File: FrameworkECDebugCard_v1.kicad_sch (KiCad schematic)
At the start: 24 parts, among them P1 USB_C_Plug_USB2.0, P2 USB_B_Micro, U1 FT230XS

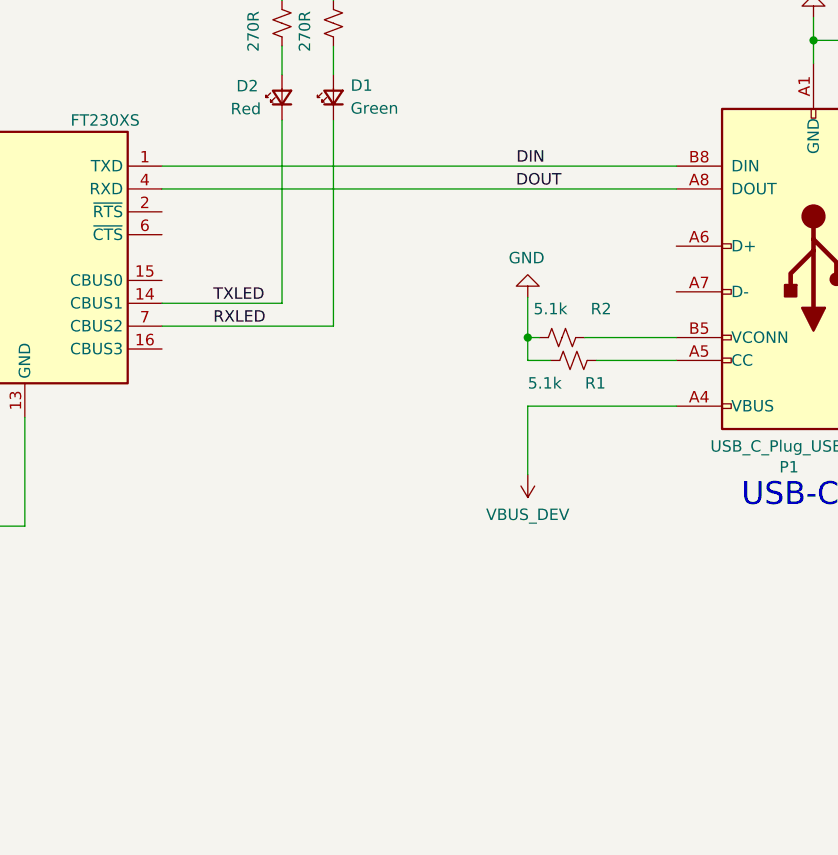
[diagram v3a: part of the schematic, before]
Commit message: Add a 1x5 header to break out the EC/FTDI pins
This header uses the SparkFun "LOCK" footprint, which should
allow me to click in a header without soldering it down.
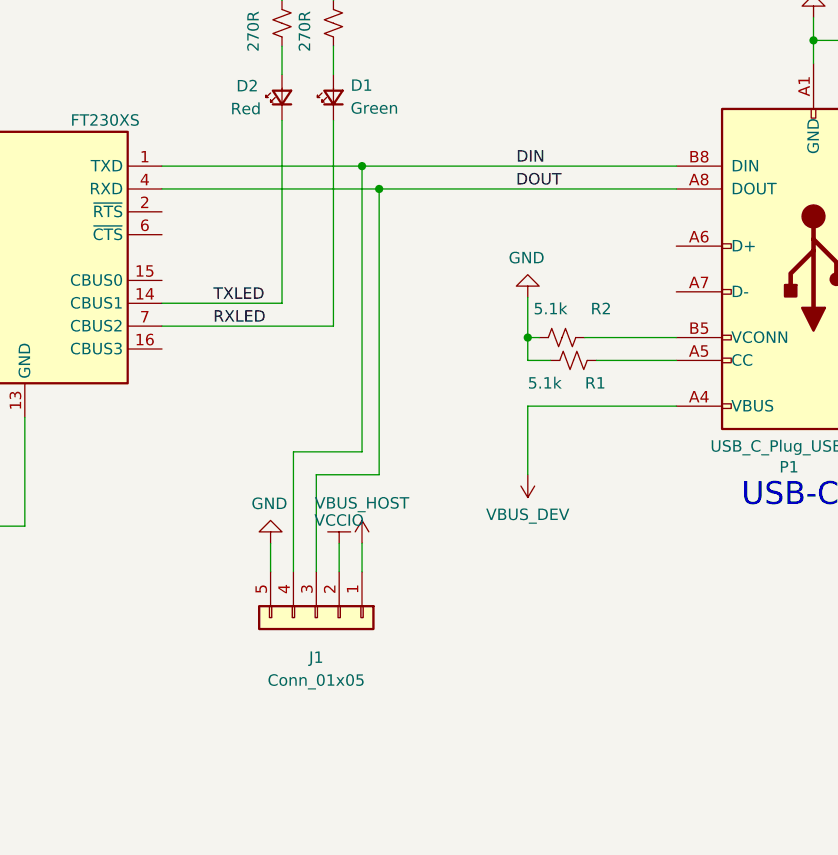
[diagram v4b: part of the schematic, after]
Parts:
- added J1: Conn_01x05, FrameworkECDebugCard_v1:1X05_LOCK, symbol Connector_Generic:Conn_01x05
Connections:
- net DIN: now also J1.4 (Pin_4)
- net DOUT: now also J1.3 (Pin_3)
- net GND: now also J1.5 (Pin_5)
- net VBUS_HOST: now also J1.1 (Pin_1)
- net VCCIO: now also J1.2 (Pin_2)
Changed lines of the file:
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@@
   (junction (at 144.145 63.5) (diameter 0) (color 0 0 0 0)
   )
+  (junction (at 127.635 46.99) (diameter 0) (color 0 0 0 0)
+  )
   (junction (at 54.61 36.83) (diameter 0) (color 0 0 0 0)
   )
@@
   (junction (at 34.925 102.87) (diameter 0) (color 0 0 0 0)
   )
+  (junction (at 125.73 44.45) (diameter 0) (color 0 0 0 0)
+  )
   (wire (pts (xy 116.84 31.115) (xy 116.84 34.29))
     (stroke (width 0) (type default) (color 0 0 0 0))
@@
     (stroke (width 0) (type default) (color 0 0 0 0))
   )
+  (wire (pts (xy 123.19 86.36) (xy 123.19 89.535))
+    (stroke (width 0) (type default) (color 0 0 0 0))
+  )
   (wire (pts (xy 67.945 57.15) (xy 62.23 57.15))
     (stroke (width 0) (type default) (color 0 0 0 0))
@@
     (stroke (width 0) (type default) (color 0 0 0 0))
   )
-  (wire (pts (xy 103.505 46.99) (xy 160.655 46.99))
+  (wire (pts (xy 103.505 46.99) (xy 127.635 46.99))
+    (stroke (width 0) (type default) (color 0 0 0 0))
+  )
+  (wire (pts (xy 125.73 86.36) (xy 125.73 89.535))
     (stroke (width 0) (type default) (color 0 0 0 0))
   )
@@
     (stroke (width 0) (type default) (color 0 0 0 0))
   )
+  (wire (pts (xy 125.73 44.45) (xy 125.73 76.2))
+    (stroke (width 0) (type default) (color 0 0 0 0))
+  )
+  (wire (pts (xy 125.73 76.2) (xy 118.11 76.2))
+    (stroke (width 0) (type default) (color 0 0 0 0))
+  )
   (wire (pts (xy 146.685 66.04) (xy 144.145 66.04))
     (stroke (width 0) (type default) (color 0 0 0 0))
@@
     (stroke (width 0) (type default) (color 0 0 0 0))
   )
+  (wire (pts (xy 115.57 86.36) (xy 115.57 89.535))
+    (stroke (width 0) (type default) (color 0 0 0 0))
+  )
   (wire (pts (xy 40.005 66.04) (xy 40.005 69.215))
     (stroke (width 0) (type default) (color 0 0 0 0))
@@
     (stroke (width 0) (type default) (color 0 0 0 0))
   )
+  (wire (pts (xy 127.635 46.99) (xy 127.635 78.74))
+    (stroke (width 0) (type default) (color 0 0 0 0))
+  )
   (wire (pts (xy 88.265 72.39) (xy 88.265 84.455))
     (stroke (width 0) (type default) (color 0 0 0 0))
@@
     (stroke (width 0) (type default) (color 0 0 0 0))
   )
-  (wire (pts (xy 103.505 44.45) (xy 160.655 44.45))
+  (wire (pts (xy 103.505 44.45) (xy 125.73 44.45))
     (stroke (width 0) (type default) (color 0 0 0 0))
   )
@@
     (stroke (width 0) (type default) (color 0 0 0 0))
   )
+  (wire (pts (xy 118.11 76.2) (xy 118.11 89.535))
+    (stroke (width 0) (type default) (color 0 0 0 0))
+  )
   (wire (pts (xy 160.655 71.12) (xy 144.145 71.12))
     (stroke (width 0) (type default) (color 0 0 0 0))
@@
     (stroke (width 0) (type default) (color 0 0 0 0))
   )
+  (wire (pts (xy 120.65 78.74) (xy 120.65 89.535))
+    (stroke (width 0) (type default) (color 0 0 0 0))
+  )
   (wire (pts (xy 45.72 46.99) (xy 55.88 46.99))
     (stroke (width 0) (type default) (color 0 0 0 0))
   )
+  (wire (pts (xy 127.635 46.99) (xy 160.655 46.99))
+    (stroke (width 0) (type default) (color 0 0 0 0))
+  )
   (wire (pts (xy 122.555 19.685) (xy 122.555 26.035))
     (stroke (width 0) (type default) (color 0 0 0 0))
@@
   )
   (wire (pts (xy 145.415 63.5) (xy 144.145 63.5))
+    (stroke (width 0) (type default) (color 0 0 0 0))
+  )
+  (wire (pts (xy 125.73 44.45) (xy 160.655 44.45))
+    (stroke (width 0) (type default) (color 0 0 0 0))
+  )
+  (wire (pts (xy 127.635 78.74) (xy 120.65 78.74))
     (stroke (width 0) (type default) (color 0 0 0 0))
   )
@@
     (pin "1")
   )
+  (symbol (lib_id "power:GND") (at 115.57 86.36 180) (unit 1)
+    (in_bom yes) (on_board yes)
+    (property "Reference" "#PWR0111" (id 0) (at 115.57 80.01 0)
+      (effects (font (size 1.27 1.27)) hide)
+    )
+    (property "Value" "GND" (id 1) (at 115.443 81.9658 0))
+    (property "Footprint" "" (id 2) (at 115.57 86.36 0)
+      (effects (font (size 1.27 1.27)) hide)
+    )
+    (property "Datasheet" "" (id 3) (at 115.57 86.36 0)
+      (effects (font (size 1.27 1.27)) hide)
+    )
+    (pin "1")
+  )
   (symbol (lib_id "Device:LED_Small") (at 116.84 36.83 90) (unit 1)
     (in_bom yes) (on_board yes)
@@
     (pin "1")
     (pin "2")
+  )
+  (symbol (lib_name "VCCIO_1") (lib_id "FrameworkECDebugCard_v1-rescue:VCCIO") (at 123.19 86.36 0) (unit 1)
+    (in_bom yes) (on_board yes)
+    (property "Reference" "#PWR0112" (id 0) (at 123.19 90.17 0)
+      (effects (font (size 1.27 1.27)) hide)
+    )
+    (property "Value" "VCCIO" (id 1) (at 123.19 83.82 0))
+    (property "Footprint" "" (id 2) (at 123.19 86.36 0)
+      (effects (font (size 1.27 1.27)) hide)
+    )
+    (property "Datasheet" "" (id 3) (at 123.19 86.36 0)
+      (effects (font (size 1.27 1.27)) hide)
+    )
+    (pin "1")
   )
   (symbol (lib_id "power:GND") (at 26.67 73.025 0) (unit 1)
@@
     (pin "2")
   )
+  (symbol (lib_id "FrameworkECDebugCard_v1-rescue:VBUS_HOST") (at 125.73 86.36 0) (unit 1)
+    (in_bom yes) (on_board yes)
+    (property "Reference" "#PWR0110" (id 0) (at 125.73 90.17 0)
+      (effects (font (size 1.27 1.27)) hide)
+    )
+    (property "Value" "VBUS_HOST" (id 1) (at 125.73 81.915 0))
+    (property "Footprint" "" (id 2) (at 125.73 86.36 0)
+      (effects (font (size 1.27 1.27)) hide)
+    )
+    (property "Datasheet" "" (id 3) (at 125.73 86.36 0)
+      (effects (font (size 1.27 1.27)) hide)
+    )
+    (pin "1")
+  )
   (symbol (lib_id "Connector:USB_B_Micro") (at 24.765 44.45 0) (unit 1)
     (in_bom yes) (on_board yes) (fields_autoplaced)
@@
     )
     (pin "1")
+  )
+  (symbol (lib_id "Connector_Generic:Conn_01x05") (at 120.65 94.615 270) (unit 1)
+    (in_bom no) (on_board yes) (fields_autoplaced)
+    (property "Reference" "J1" (id 0) (at 120.65 99.06 90))
+    (property "Value" "Conn_01x05" (id 1) (at 120.65 101.6 90))
+    (property "Footprint" "FrameworkECDebugCard_v1:1X05_LOCK" (id 2) (at 120.65 94.615 0)
+      (effects (font (size 1.27 1.27)) hide)
+    )
+    (property "Datasheet" "~" (id 3) (at 120.65 94.615 0)
+      (effects (font (size 1.27 1.27)) hide)
+    )
+    (pin "1")
+    (pin "2")
+    (pin "3")
+    (pin "4")
+    (pin "5")
   )
   (symbol (lib_id "Device:C_Small") (at 41.91 111.125 0) (unit 1)
@@
       (reference "#PWR0109") (unit 1) (value "VBUS_HOST") (footprint "")
     )
+    (path "/972f110e-25e6-42e3-895b-1f08816f389b"
+      (reference "#PWR0110") (unit 1) (value "VBUS_HOST") (footprint "")
+    )
+    (path "/0cefe424-2c69-440e-bfa1-43f7b326a942"
+      (reference "#PWR0111") (unit 1) (value "GND") (footprint "")
+    )
+    (path "/41397ac6-deec-4684-a1fe-fc97df4bb74d"
+      (reference "#PWR0112") (unit 1) (value "VCCIO") (footprint "")
+    )
     (path "/e4410938-748d-4f87-a5a0-2f41e55e999c"
       (reference "C1") (unit 1) (value "100nf") (footprint "Capacitor_SMD:C_0402_1005Metric")
@@
       (reference "H2") (unit 1) (value "MountingHole") (footprint "MountingHole:MountingHole_2.2mm_M2")
     )
+    (path "/d0726bc2-9333-4c1c-8a2c-af2615eef0e6"
+      (reference "J1") (unit 1) (value "Conn_01x05") (footprint "FrameworkECDebugCard_v1:1X05_LOCK")
+    )
     (path "/00000000-0000-0000-0000-00005fd76bc6"

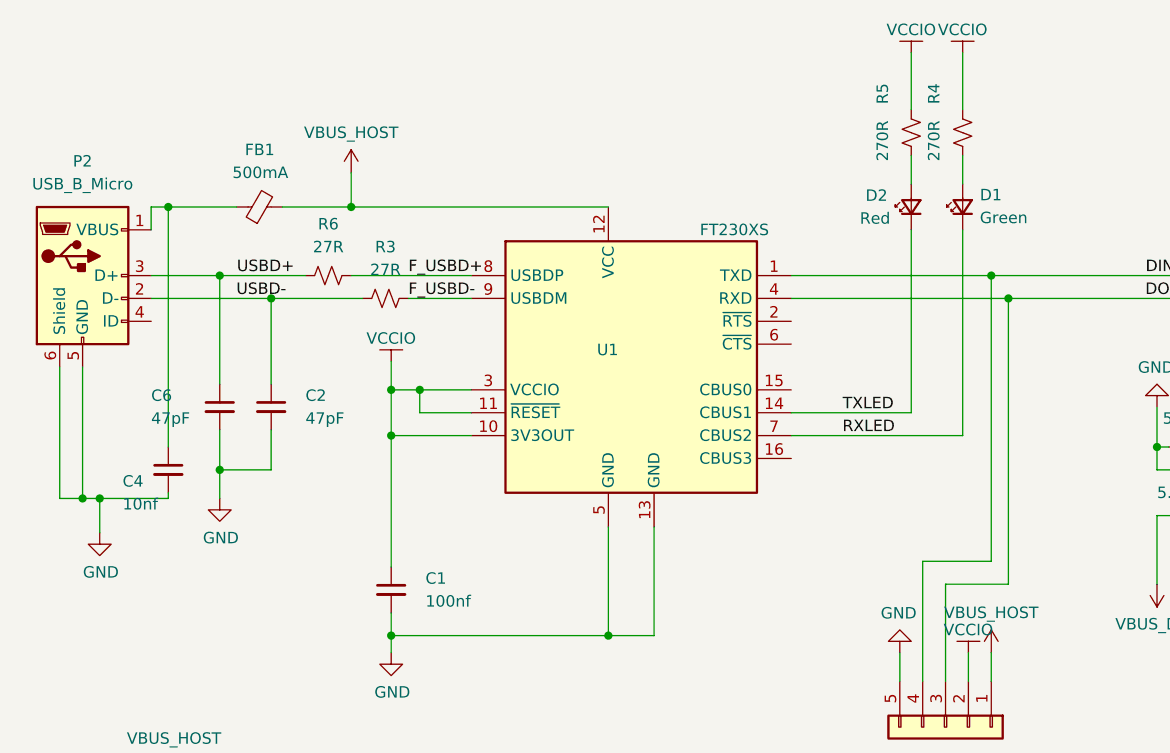
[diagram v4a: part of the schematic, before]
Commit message: Re-route everything to avoid B.Cu cuts across diff pair
Switched the positions of the TX and RX LEDs to match which side of the
chip they're on. Significantly re-routed TX/RX. Added via stitching.

The ground planes are much more contiguous, except for U1 pad 5 which
connects to GND on the back with a via.

(Kieran's suggestion was to remove the lines on the back that cut
horizontally across the differential pair; I don't know if having
RXLED's sink next to the diff pair will be a problem.)

Re-version the card to "EC Card 2"
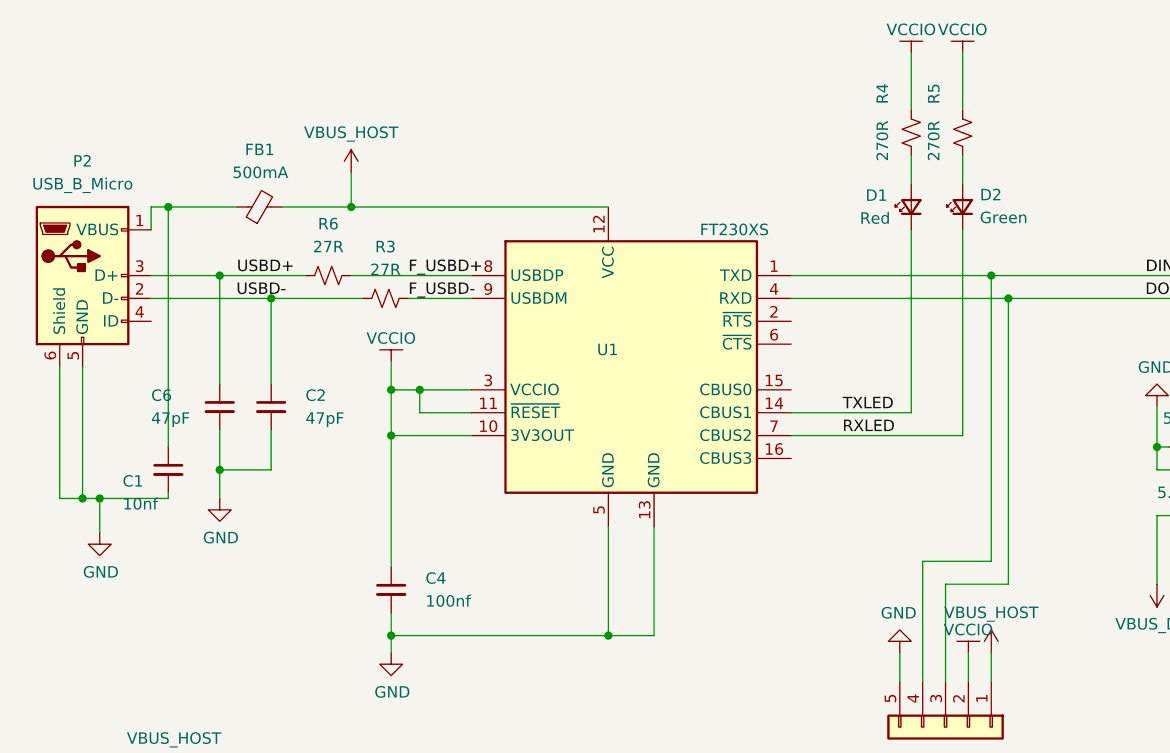
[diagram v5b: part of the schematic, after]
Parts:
- renumbered C4 to C1, C1 to C4, D2 to D1, D1 to D2, R5 to R4, R4 to R5
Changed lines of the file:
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@@
   (symbol (lib_id "Device:LED_Small") (at 116.84 36.83 90) (unit 1)
     (in_bom yes) (on_board yes)
-    (property "Reference" "D2" (id 0) (at 111.76 35.56 90)
+    (property "Reference" "D1" (id 0) (at 111.76 35.56 90)
       (effects (font (size 1.27 1.27)) (justify right))
     )
@@
   (symbol (lib_id "Device:LED_Small") (at 122.555 36.83 90) (unit 1)
     (in_bom yes) (on_board yes) (fields_autoplaced)
-    (property "Reference" "D1" (id 0) (at 124.46 35.4964 90)
+    (property "Reference" "D2" (id 0) (at 124.46 35.4964 90)
       (effects (font (size 1.27 1.27)) (justify right))
     )
@@
   (symbol (lib_id "Device:R_Small_US") (at 116.84 28.575 0) (unit 1)
     (in_bom yes) (on_board yes)
-    (property "Reference" "R5" (id 0) (at 113.665 25.4 90)
+    (property "Reference" "R4" (id 0) (at 113.665 25.4 90)
       (effects (font (size 1.27 1.27)) (justify left))
     )
@@
   (symbol (lib_id "Device:C_Small") (at 59.055 79.375 0) (unit 1)
     (in_bom yes) (on_board yes) (fields_autoplaced)
-    (property "Reference" "C1" (id 0) (at 62.865 78.1049 0)
+    (property "Reference" "C4" (id 0) (at 62.865 78.1049 0)
       (effects (font (size 1.27 1.27)) (justify left))
     )
@@
   (symbol (lib_id "Device:C_Small") (at 34.29 66.04 0) (unit 1)
     (in_bom yes) (on_board yes)
-    (property "Reference" "C4" (id 0) (at 29.21 67.31 0)
+    (property "Reference" "C1" (id 0) (at 29.21 67.31 0)
       (effects (font (size 1.27 1.27)) (justify left))
     )
@@
   (symbol (lib_id "Device:R_Small_US") (at 122.555 28.575 0) (unit 1)
     (in_bom yes) (on_board yes)
-    (property "Reference" "R4" (id 0) (at 119.38 25.4 90)
+    (property "Reference" "R5" (id 0) (at 119.38 25.4 90)
       (effects (font (size 1.27 1.27)) (justify left))
     )
@@
       (reference "#PWR0112") (unit 1) (value "VCCIO") (footprint "")
     )
-    (path "/e4410938-748d-4f87-a5a0-2f41e55e999c"
-      (reference "C1") (unit 1) (value "100nf") (footprint "Capacitor_SMD:C_0402_1005Metric")
+    (path "/e88ed97c-5f7f-4fa6-b202-1f3880388383"
+      (reference "C1") (unit 1) (value "10nf") (footprint "Capacitor_SMD:C_0402_1005Metric")
     )
     (path "/685f0971-12c4-4d07-8eec-3ff16ff9a7d3"
@@
       (reference "C3") (unit 1) (value "100nf") (footprint "Capacitor_SMD:C_0402_1005Metric")
     )
-    (path "/e88ed97c-5f7f-4fa6-b202-1f3880388383"
-      (reference "C4") (unit 1) (value "10nf") (footprint "Capacitor_SMD:C_0402_1005Metric")
+    (path "/e4410938-748d-4f87-a5a0-2f41e55e999c"
+      (reference "C4") (unit 1) (value "100nf") (footprint "Capacitor_SMD:C_0402_1005Metric")
     )
     (path "/d393b8c4-8105-4600-aeed-08d8efde382f"
@@
       (reference "C6") (unit 1) (value "47pF") (footprint "Capacitor_SMD:C_0402_1005Metric")
     )
+    (path "/2326b3ba-1742-4f36-87f7-22991a003d68"
+      (reference "D1") (unit 1) (value "Red") (footprint "LED_SMD:LED_0603_1608Metric")
+    )
     (path "/951a9737-1abd-4cc1-a961-022d0a301f2c"
-      (reference "D1") (unit 1) (value "Green") (footprint "LED_SMD:LED_0603_1608Metric")
-    )
-    (path "/2326b3ba-1742-4f36-87f7-22991a003d68"
-      (reference "D2") (unit 1) (value "Red") (footprint "LED_SMD:LED_0603_1608Metric")
+      (reference "D2") (unit 1) (value "Green") (footprint "LED_SMD:LED_0603_1608Metric")
     )
     (path "/91d38762-eed1-4640-8cf2-f727d0ea908c"
@@
       (reference "R3") (unit 1) (value "27R") (footprint "Resistor_SMD:R_0402_1005Metric")
     )
+    (path "/dd063de5-da3d-49de-a899-532aa51b8a7c"
+      (reference "R4") (unit 1) (value "270R") (footprint "Resistor_SMD:R_0402_1005Metric")
+    )
     (path "/f4b69b4c-b4ac-4a4e-8c9e-77f4e7698670"
-      (reference "R4") (unit 1) (value "270R") (footprint "Resistor_SMD:R_0402_1005Metric")
-    )
-    (path "/dd063de5-da3d-49de-a899-532aa51b8a7c"
       (reference "R5") (unit 1) (value "270R") (footprint "Resistor_SMD:R_0402_1005Metric")
     )

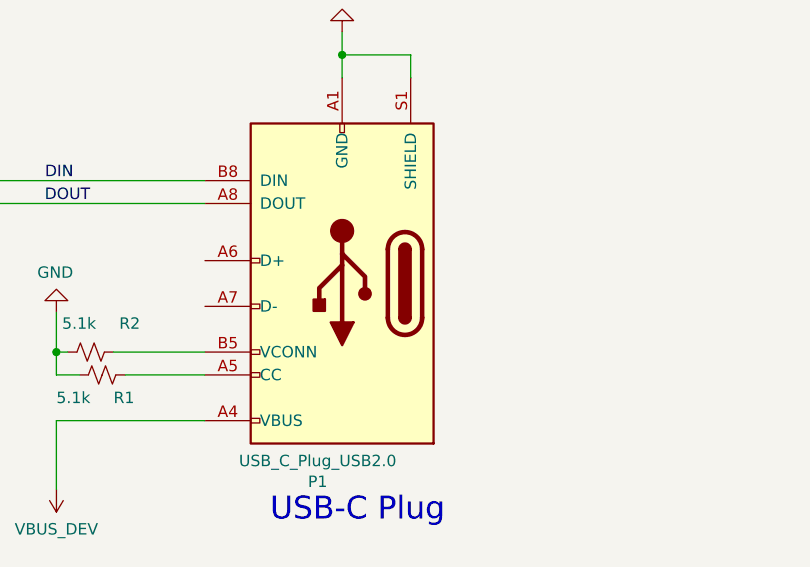
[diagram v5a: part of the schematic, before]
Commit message: sch: update to kicad 8
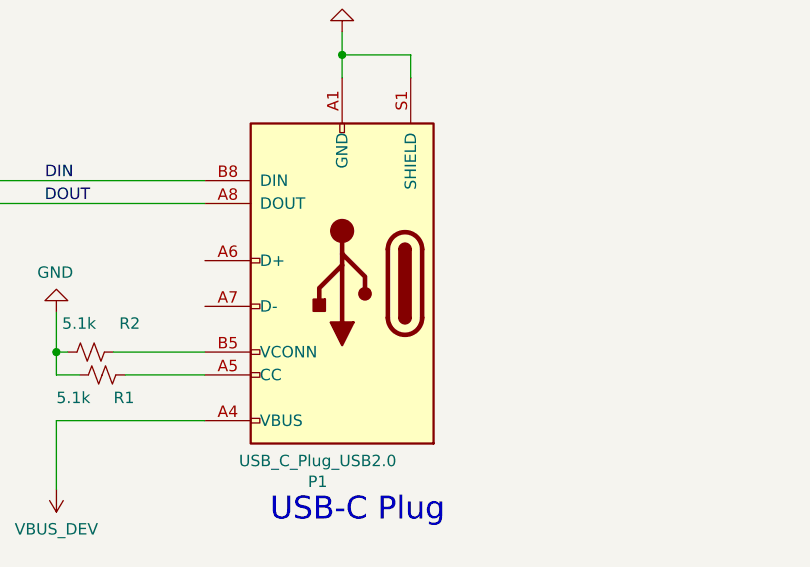
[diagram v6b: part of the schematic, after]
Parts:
- R1: Spice_Model 5.1k -> (none); Spice_Netlist_Enabled Y -> (none); Spice_Primitive R -> (none)
